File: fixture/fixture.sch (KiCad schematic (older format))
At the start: 40 parts, among them J1 Conn_Coaxial, J10 Conn_Coaxial, J11 Conn_Coaxial, J12 Conn_Coaxial, J13 Conn_Coaxial, J14 Conn_Coaxial, J15 Conn_Coaxial, J16 Conn_Coaxial, J17 Conn_Coaxial, J18 Conn_01x01, J19 Conn_01x01, J2 Conn_Coaxial, J20 Conn_01x01, J21 Conn_01x01, J22 Conn_Coaxial, J23 Conn_Coaxial, J24 Conn_Coaxial, J25 Conn_Coaxial, J26 Conn_01x02, J27 Conn_Coaxial, J28 Conn_01x02, J29 Conn_Coaxial, J3 Conn_Coaxial, J30 Conn_01x01, J31 Conn_01x01, J32 Conn_Coaxial, J4 Conn_02x08_Counter_Clockwise, J5 Conn_02x08_Counter_Clockwise, J6 Conn_Coaxial, J7 Conn_Coaxial, J8 Conn_Coaxial, J9 Conn_Coaxial

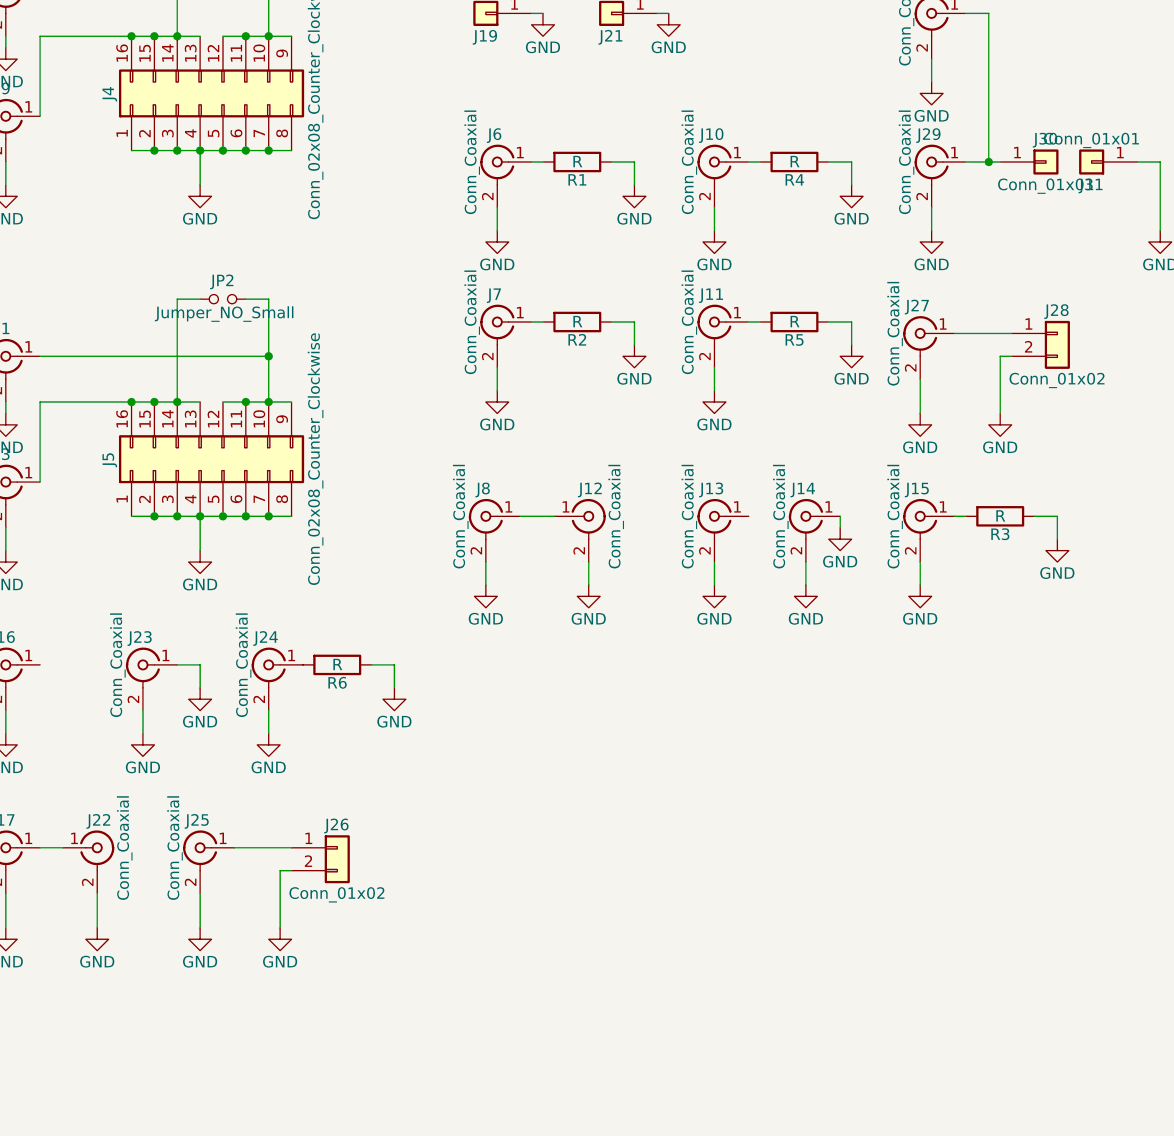
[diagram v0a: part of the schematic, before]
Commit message: Made more room for handle of ZIF socket
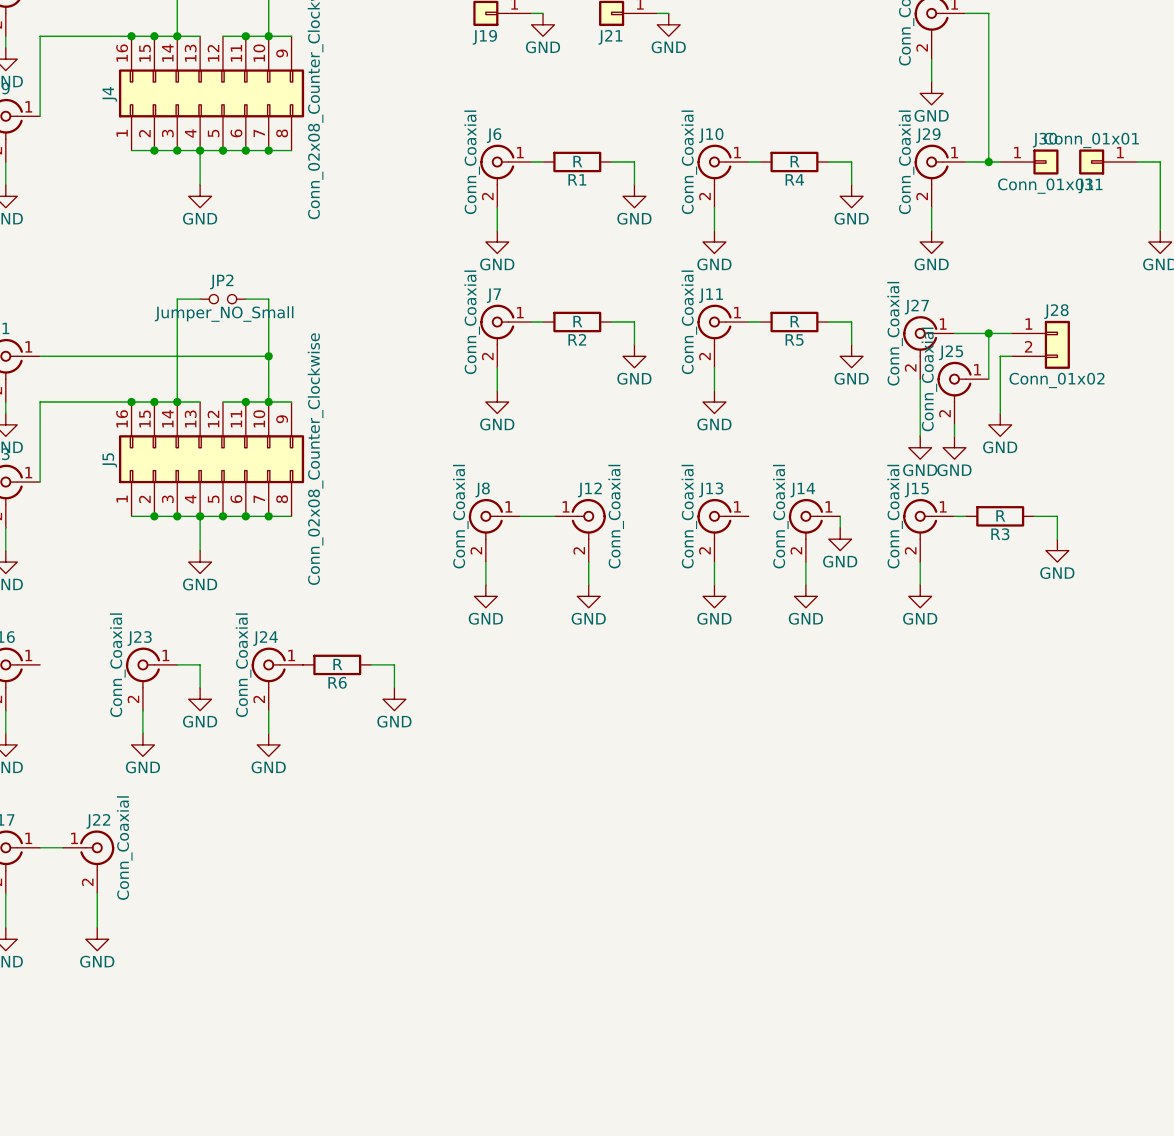
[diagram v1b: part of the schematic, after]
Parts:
- removed J26: Conn_01x02, Connectors_Terminal_Blocks:TerminalBlock_bornier-2_P5.08mm, symbol Conn_01x02
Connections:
- net at J25.1 (In): now also J27.1 (In), J28.1 (Pin_1)
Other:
- moved on the sheet: J25

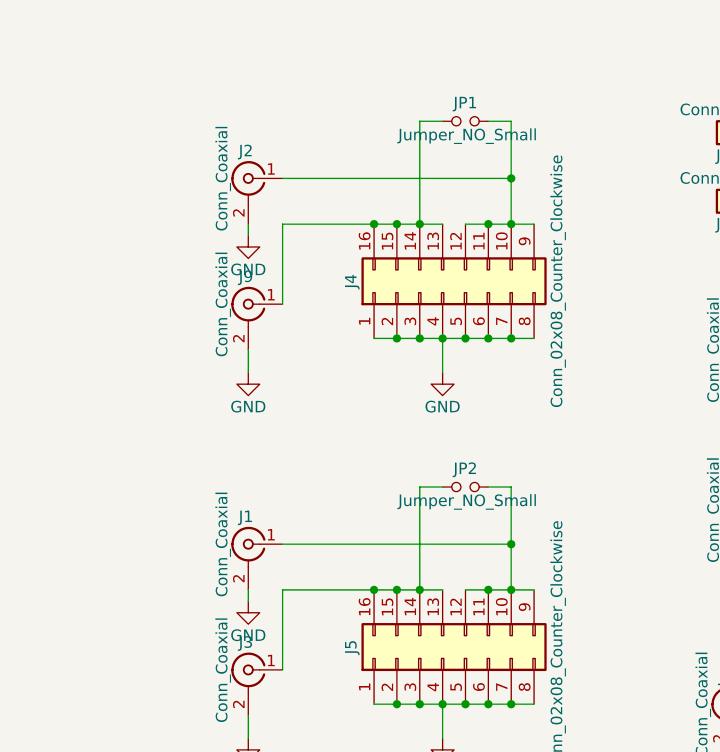
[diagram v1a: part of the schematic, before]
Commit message: Added vacuum holes to fixture
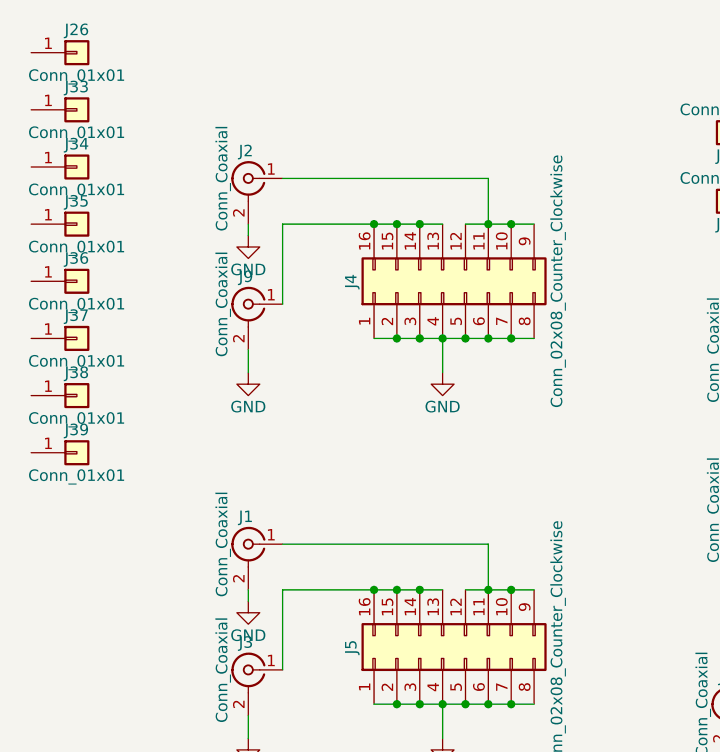
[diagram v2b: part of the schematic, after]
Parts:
- removed JP1, JP2: Jumper_NO_Small, Pin_Headers:Pin_Header_Straight_1x02_Pitch2.54mm, symbol Jumper_NO_Small
- added J26, J33, J34, J35, J36, J37, J38, J39: Conn_01x01, fixture:AirHole, symbol Conn_01x01

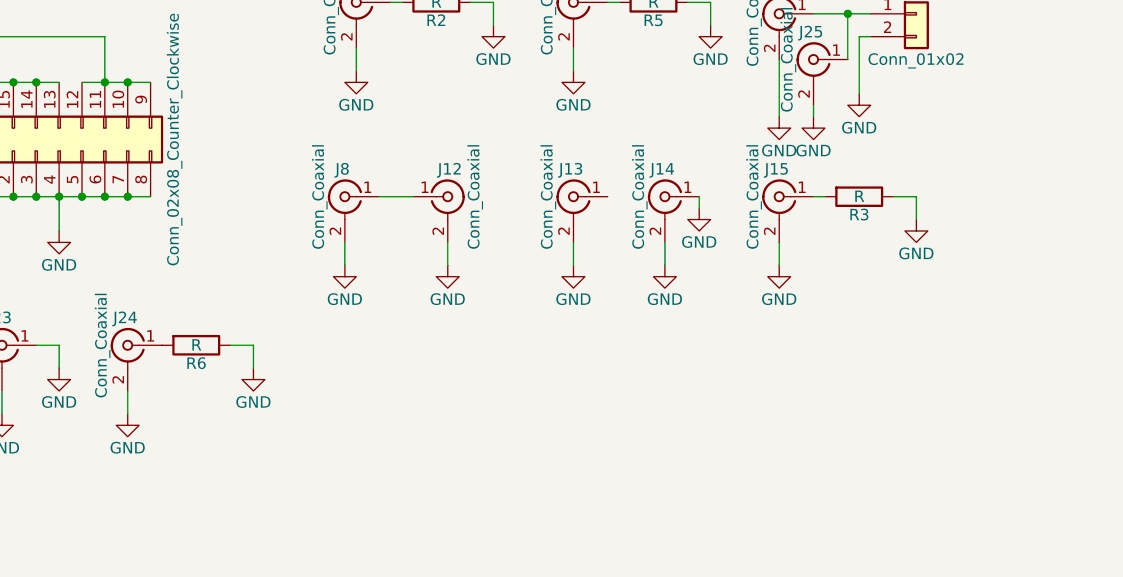
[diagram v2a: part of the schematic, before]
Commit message: Modified fixture for larger holes for ZIF socket
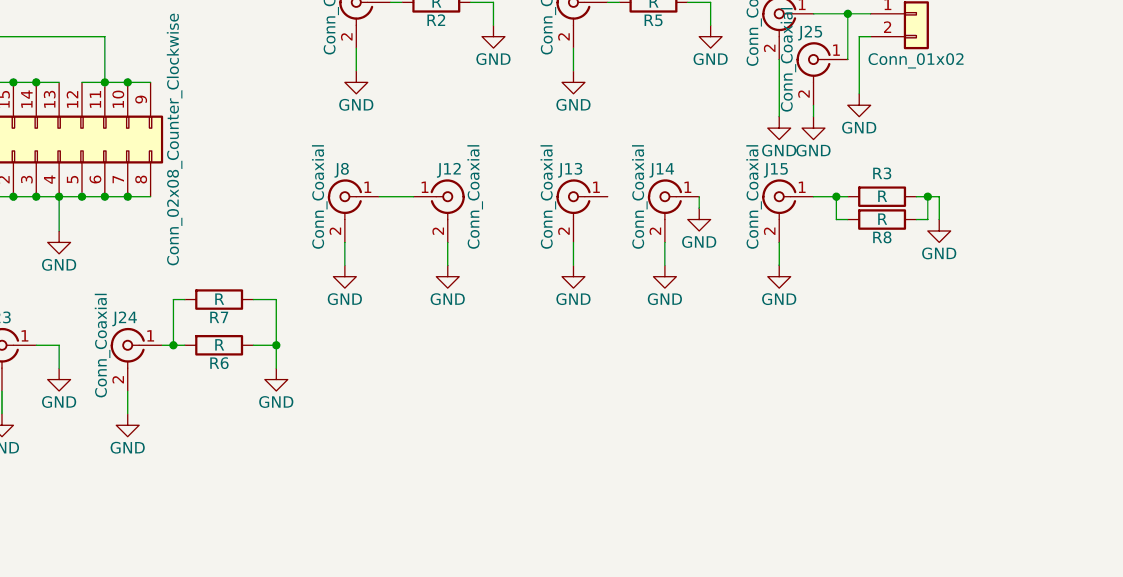
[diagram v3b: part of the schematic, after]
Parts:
- added R7, R8: R, Resistors_SMD:R_0805_HandSoldering, symbol R
- J4, J5: footprint Housings_DIP:DIP-16_W7.62mm_Socket_LongPads -> fixture:ZIFSocket16pin
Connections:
- net GND: now also R7.1, R8.1
- net at J15.1 (In), R3.2: now also R8.2
- net at J24.1 (In), R6.2: now also R7.2
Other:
- moved on the sheet: R3, R6
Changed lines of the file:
@@
 F 0 "J4" H 2550 2250 50  0000 C CNN
 F 1 "Conn_02x08_Counter_Clockwise" H 2550 1350 50  0000 C CNN
-F 2 "Housings_DIP:DIP-16_W7.62mm_Socket_LongPads" H 2500 1850 50  0001 C CNN
+F 2 "fixture:ZIFSocket16pin" H 2500 1850 50  0001 C CNN
 F 3 "" H 2500 1850 50  0001 C CNN
 	1    2500 1850
@@
 F 0 "J5" H 2550 3850 50  0000 C CNN
 F 1 "Conn_02x08_Counter_Clockwise" H 2550 2950 50  0000 C CNN
-F 2 "Housings_DIP:DIP-16_W7.62mm_Socket_LongPads" H 2500 3450 50  0001 C CNN
+F 2 "fixture:ZIFSocket16pin" H 2500 3450 50  0001 C CNN
 F 3 "" H 2500 3450 50  0001 C CNN
 	1    2500 3450
@@
 L R R3
 U 1 1 5DAFE6CB
-P 6000 3650
-F 0 "R3" V 6080 3650 50  0000 C CNN
-F 1 "R" V 6000 3650 50  0000 C CNN
-F 2 "Resistors_SMD:R_0805_HandSoldering" V 5930 3650 50  0001 C CNN
-F 3 "" H 6000 3650 50  0001 C CNN
-	1    6000 3650
+P 6100 3650
+F 0 "R3" V 6000 3650 50  0000 C CNN
+F 1 "R" V 6100 3650 50  0000 C CNN
+F 2 "Resistors_SMD:R_0805_HandSoldering" V 6030 3650 50  0001 C CNN
+F 3 "" H 6100 3650 50  0001 C CNN
+	1    6100 3650
 	0    1    1    0
 $EndComp
@@
 L GND #PWR37
 U 1 1 5DAFE6D1
-P 6250 3750
-F 0 "#PWR37" H 6250 3500 50  0001 C CNN
-F 1 "GND" H 6250 3600 50  0000 C CNN
-F 2 "" H 6250 3750 50  0001 C CNN
-F 3 "" H 6250 3750 50  0001 C CNN
-	1    6250 3750
+P 6350 3750
+F 0 "#PWR37" H 6350 3500 50  0001 C CNN
+F 1 "GND" H 6350 3600 50  0000 C CNN
+F 2 "" H 6350 3750 50  0001 C CNN
+F 3 "" H 6350 3750 50  0001 C CNN
+	1    6350 3750
 	1    0    0    -1
 $EndComp
@@
 L R R6
 U 1 1 5DAFEEF3
-P 3100 4300
-F 0 "R6" V 3180 4300 50  0000 C CNN
-F 1 "R" V 3100 4300 50  0000 C CNN
-F 2 "Resistors_SMD:R_0805_HandSoldering" V 3030 4300 50  0001 C CNN
-F 3 "" H 3100 4300 50  0001 C CNN
-	1    3100 4300
+P 3200 4300
+F 0 "R6" V 3280 4300 50  0000 C CNN
+F 1 "R" V 3200 4300 50  0000 C CNN
+F 2 "Resistors_SMD:R_0805_HandSoldering" V 3130 4300 50  0001 C CNN
+F 3 "" H 3200 4300 50  0001 C CNN
+	1    3200 4300
 	0    1    1    0
 $EndComp
@@
 L GND #PWR13
 U 1 1 5DAFEEF9
-P 3350 4400
-F 0 "#PWR13" H 3350 4150 50  0001 C CNN
-F 1 "GND" H 3350 4250 50  0000 C CNN
-F 2 "" H 3350 4400 50  0001 C CNN
-F 3 "" H 3350 4400 50  0001 C CNN
-	1    3350 4400
+P 3450 4400
+F 0 "#PWR13" H 3450 4150 50  0001 C CNN
+F 1 "GND" H 3450 4250 50  0000 C CNN
+F 2 "" H 3450 4400 50  0001 C CNN
+F 3 "" H 3450 4400 50  0001 C CNN
+	1    3450 4400
 	1    0    0    -1
 $EndComp
@@
 	5650 3950 5650 3850
 Wire Wire Line
-	6250 3750 6250 3650
-Wire Wire Line
-	6250 3650 6150 3650
-Wire Wire Line
-	5850 3650 5800 3650
+	6350 3750 6350 3650
+Wire Wire Line
+	6350 3650 6250 3650
+Wire Wire Line
+	5800 3650 5950 3650
 Wire Wire Line
 	1650 4600 1650 4500
@@
 	2800 4600 2800 4500
 Wire Wire Line
-	3350 4400 3350 4300
-Wire Wire Line
-	3350 4300 3250 4300
+	3450 4100 3450 4400
+Wire Wire Line
+	3450 4300 3350 4300
 Wire Wire Line
 	1650 5300 1650 5450
@@
 	1    0    0    -1
 $EndComp
+$Comp
+L R R7
+U 1 1 5DC5B743
+P 3200 4100
+F 0 "R7" V 3280 4100 50  0000 C CNN
+F 1 "R" V 3200 4100 50  0000 C CNN
+F 2 "Resistors_SMD:R_0805_HandSoldering" V 3130 4100 50  0001 C CNN
+F 3 "" H 3200 4100 50  0001 C CNN
+	1    3200 4100
+	0    1    1    0
+$EndComp
+Wire Wire Line
+	3050 4300 2950 4300
+Wire Wire Line
+	3000 4300 3000 4100
+Wire Wire Line
+	3000 4100 3050 4100
+Connection ~ 3000 4300
+Wire Wire Line
+	3350 4100 3450 4100
+Connection ~ 3450 4300
+$Comp
+L R R8
+U 1 1 5DC5BB65
+P 6100 3750
+F 0 "R8" V 6180 3750 50  0000 C CNN
+F 1 "R" V 6100 3750 50  0000 C CNN
+F 2 "Resistors_SMD:R_0805_HandSoldering" V 6030 3750 50  0001 C CNN
+F 3 "" H 6100 3750 50  0001 C CNN
+	1    6100 3750
+	0    1    1    0
+$EndComp
+Wire Wire Line
+	5900 3650 5900 3750
+Wire Wire Line
+	5900 3750 5950 3750
+Connection ~ 5900 3650
+Wire Wire Line
+	6300 3650 6300 3750
+Wire Wire Line
+	6300 3750 6250 3750
+Connection ~ 6300 3650
 $EndSCHEMATC

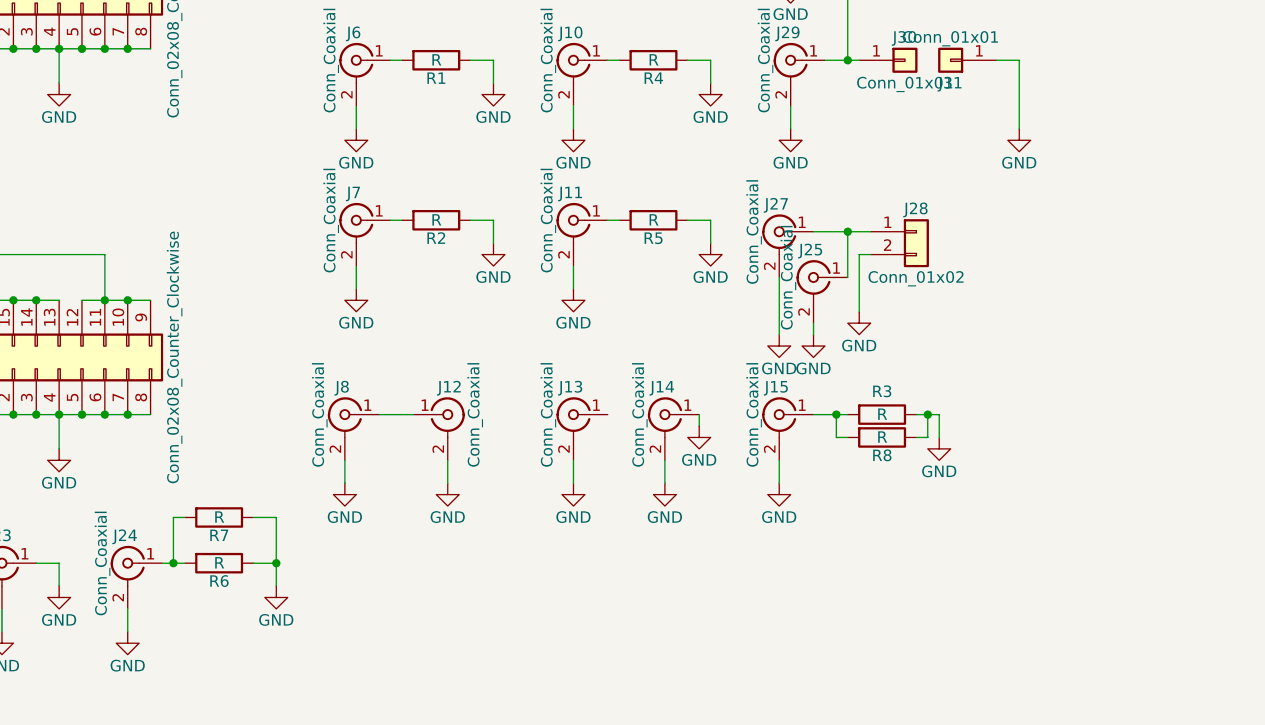
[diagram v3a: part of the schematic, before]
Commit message: Move components around on board, adjusted fixture, added touchscreen disables
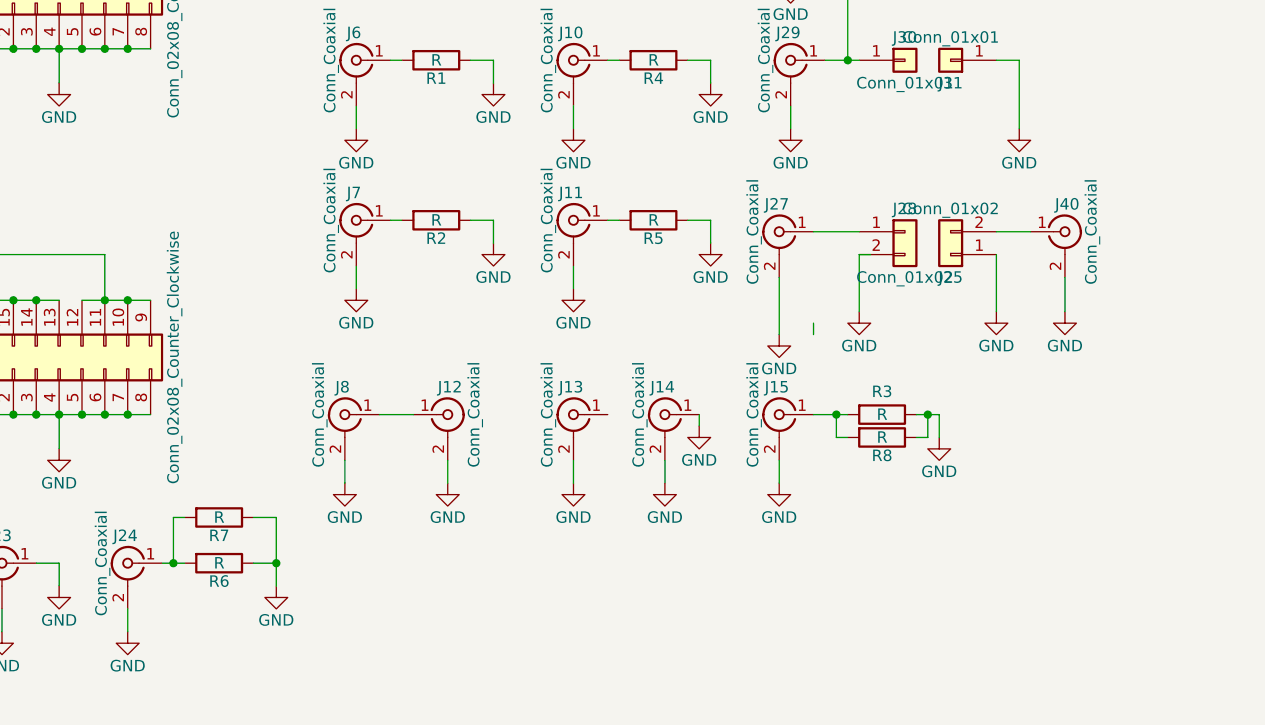
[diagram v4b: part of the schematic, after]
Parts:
- removed J25: Conn_Coaxial, Connectors:bnc-ci, symbol Conn_Coaxial
- added J25: Conn_01x02, Connectors_Terminal_Blocks:TerminalBlock_bornier-2_P5.08mm, symbol Conn_01x02
- added J40: Conn_Coaxial, fixture:Amphenol_RF_SMA_132289, symbol Conn_Coaxial
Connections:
- wire segments 79 -> 81
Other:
- moved on the sheet: J28
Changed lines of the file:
@@
 $EndComp
 $Comp
-L GND #PWR37
+L GND #PWR36
 U 1 1 5DAFE6D1
 P 6350 3750
-F 0 "#PWR37" H 6350 3500 50  0001 C CNN
+F 0 "#PWR36" H 6350 3500 50  0001 C CNN
 F 1 "GND" H 6350 3600 50  0000 C CNN
 F 2 "" H 6350 3750 50  0001 C CNN
@@
 	5650 3950 5650 3850
 Wire Wire Line
-	6350 3750 6350 3650
-Wire Wire Line
-	6350 3650 6250 3650
+	6350 3650 6350 3750
+Wire Wire Line
+	6250 3650 6350 3650
 Wire Wire Line
 	5800 3650 5950 3650
@@
 Wire Wire Line
 	1900 5100 1800 5100
-$Comp
-L Conn_Coaxial J25
-U 1 1 5DAFF730
-P 5800 3050
-F 0 "J25" H 5810 3170 50  0000 C CNN
-F 1 "Conn_Coaxial" V 5915 3050 50  0000 C CNN
-F 2 "Connectors:bnc-ci" H 5800 3050 50  0001 C CNN
-F 3 "" H 5800 3050 50  0001 C CNN
-	1    5800 3050
-	-1   0    0    -1
-$EndComp
 $Comp
 L Conn_Coaxial J27
@@
 L Conn_01x02 J28
 U 1 1 5DAFFC44
-P 6250 2850
-F 0 "J28" H 6250 2950 50  0000 C CNN
-F 1 "Conn_01x02" H 6250 2650 50  0000 C CNN
-F 2 "Connectors_Terminal_Blocks:TerminalBlock_bornier-2_P5.08mm" H 6250 2850 50  0001 C CNN
-F 3 "" H 6250 2850 50  0001 C CNN
-	1    6250 2850
-	1    0    0    -1
-$EndComp
-$Comp
-L GND #PWR36
+P 6200 2850
+F 0 "J28" H 6200 2950 50  0000 C CNN
+F 1 "Conn_01x02" H 6200 2650 50  0000 C CNN
+F 2 "Connectors_Terminal_Blocks:TerminalBlock_bornier-2_P5.08mm" H 6200 2850 50  0001 C CNN
+F 3 "" H 6200 2850 50  0001 C CNN
+	1    6200 2850
+	1    0    0    -1
+$EndComp
+$Comp
+L GND #PWR35
 U 1 1 5DAFFC4A
 P 6000 3200
-F 0 "#PWR36" H 6000 2950 50  0001 C CNN
+F 0 "#PWR35" H 6000 2950 50  0001 C CNN
 F 1 "GND" H 6000 3050 50  0000 C CNN
 F 2 "" H 6000 3200 50  0001 C CNN
@@
 Wire Wire Line
 	6000 2950 6050 2950
-Wire Wire Line
-	5800 2850 6050 2850
 $Comp
 L GND #PWR31
@@
 Connection ~ 5950 2100
 Wire Wire Line
-	5950 3050 5950 2850
-Connection ~ 5950 2850
-$Comp
-L GND #PWR35
-U 1 1 5DAFEBBE
-P 5800 3300
-F 0 "#PWR35" H 5800 3050 50  0001 C CNN
-F 1 "GND" H 5800 3150 50  0000 C CNN
-F 2 "" H 5800 3300 50  0001 C CNN
-F 3 "" H 5800 3300 50  0001 C CNN
-	1    5800 3300
-	1    0    0    -1
-$EndComp
-Wire Wire Line
 	5800 3300 5800 3250
 Wire Wire Line
@@
 $EndComp
 Wire Wire Line
-	3050 4300 2950 4300
+	2950 4300 3050 4300
 Wire Wire Line
 	3000 4300 3000 4100
@@
 	6300 3750 6250 3750
 Connection ~ 6300 3650
+$Comp
+L Conn_Coaxial J40
+U 1 1 5DCF6605
+P 6900 2850
+F 0 "J40" H 6910 2970 50  0000 C CNN
+F 1 "Conn_Coaxial" V 7015 2850 50  0000 C CNN
+F 2 "fixture:Amphenol_RF_SMA_132289" H 6900 2850 50  0001 C CNN
+F 3 "" H 6900 2850 50  0001 C CNN
+	1    6900 2850
+	1    0    0    -1
+$EndComp
+$Comp
+L Conn_01x02 J25
+U 1 1 5DCF681B
+P 6400 2950
+F 0 "J25" H 6400 3050 50  0000 C CNN
+F 1 "Conn_01x02" H 6400 2750 50  0000 C CNN
+F 2 "Connectors_Terminal_Blocks:TerminalBlock_bornier-2_P5.08mm" H 6400 2950 50  0001 C CNN
+F 3 "" H 6400 2950 50  0001 C CNN
+	1    6400 2950
+	-1   0    0    1
+$EndComp
+Wire Wire Line
+	6750 2850 6600 2850
+$Comp
+L GND #PWR37
+U 1 1 5DCF6ABC
+P 6600 3200
+F 0 "#PWR37" H 6600 2950 50  0001 C CNN
+F 1 "GND" H 6600 3050 50  0000 C CNN
+F 2 "" H 6600 3200 50  0001 C CNN
+F 3 "" H 6600 3200 50  0001 C CNN
+	1    6600 3200
+	1    0    0    -1
+$EndComp
+Wire Wire Line
+	6600 3200 6600 2950
+$Comp
+L GND #PWR39
+U 1 1 5DCF6C59
+P 6900 3200
+F 0 "#PWR39" H 6900 2950 50  0001 C CNN
+F 1 "GND" H 6900 3050 50  0000 C CNN
+F 2 "" H 6900 3200 50  0001 C CNN
+F 3 "" H 6900 3200 50  0001 C CNN
+	1    6900 3200
+	1    0    0    -1
+$EndComp
+Wire Wire Line
+	6900 3200 6900 3050
+Wire Wire Line
+	6000 2850 5800 2850
 $EndSCHEMATC
